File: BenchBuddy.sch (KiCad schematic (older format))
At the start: 0 parts

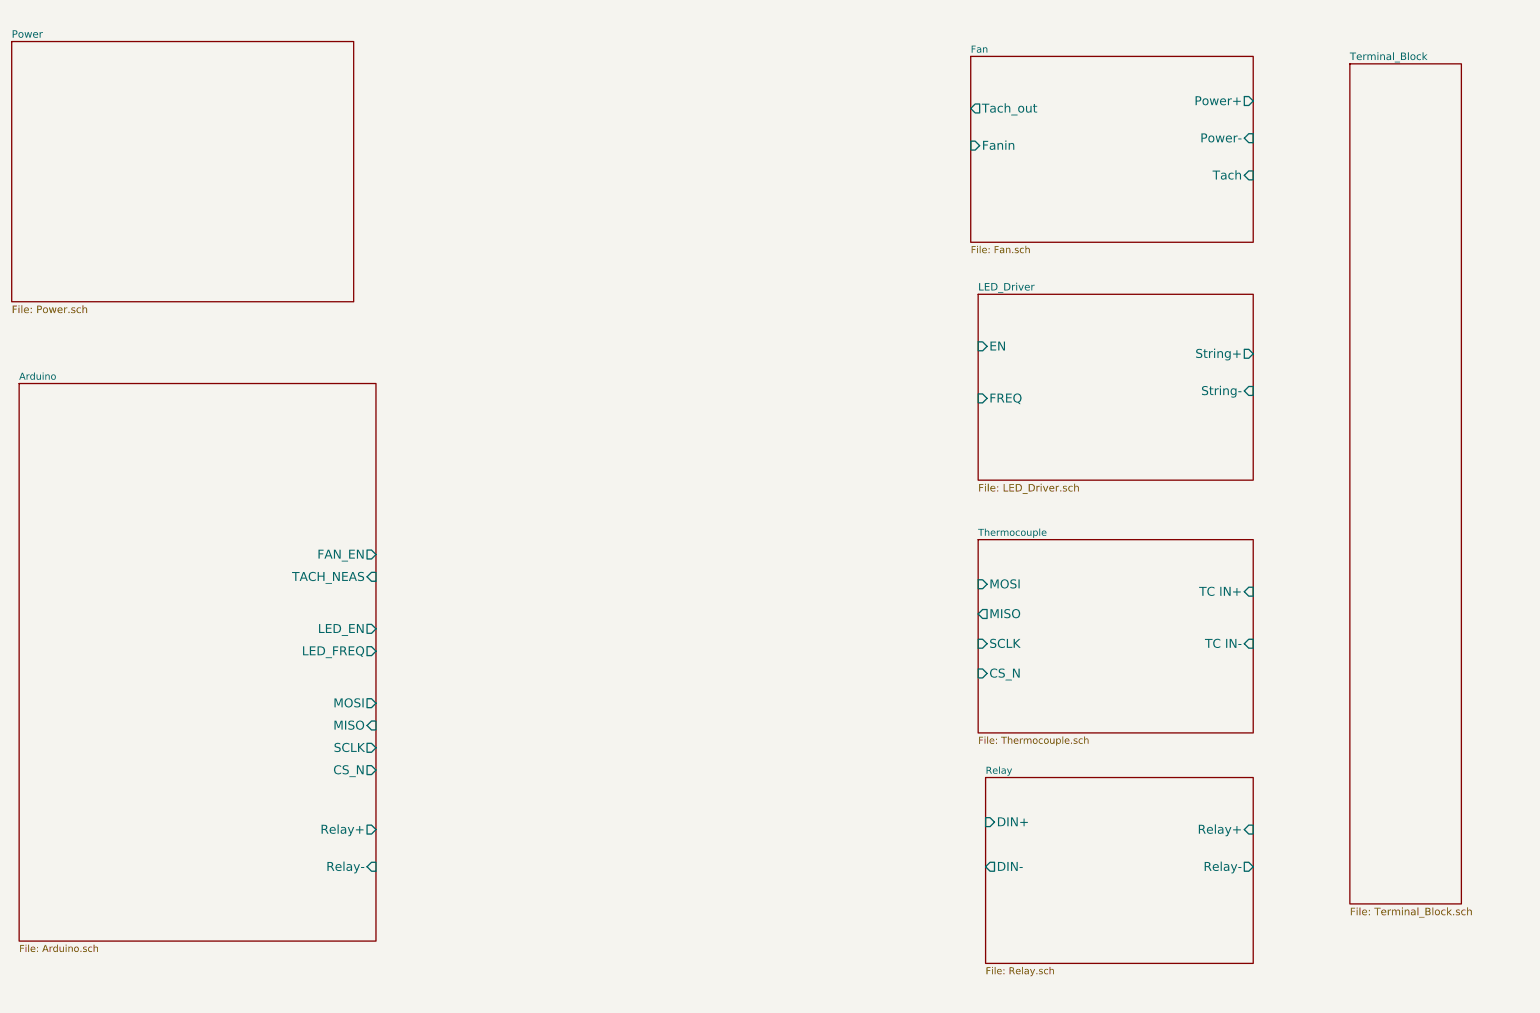
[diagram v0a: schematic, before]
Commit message: Added Powercontrol stuff
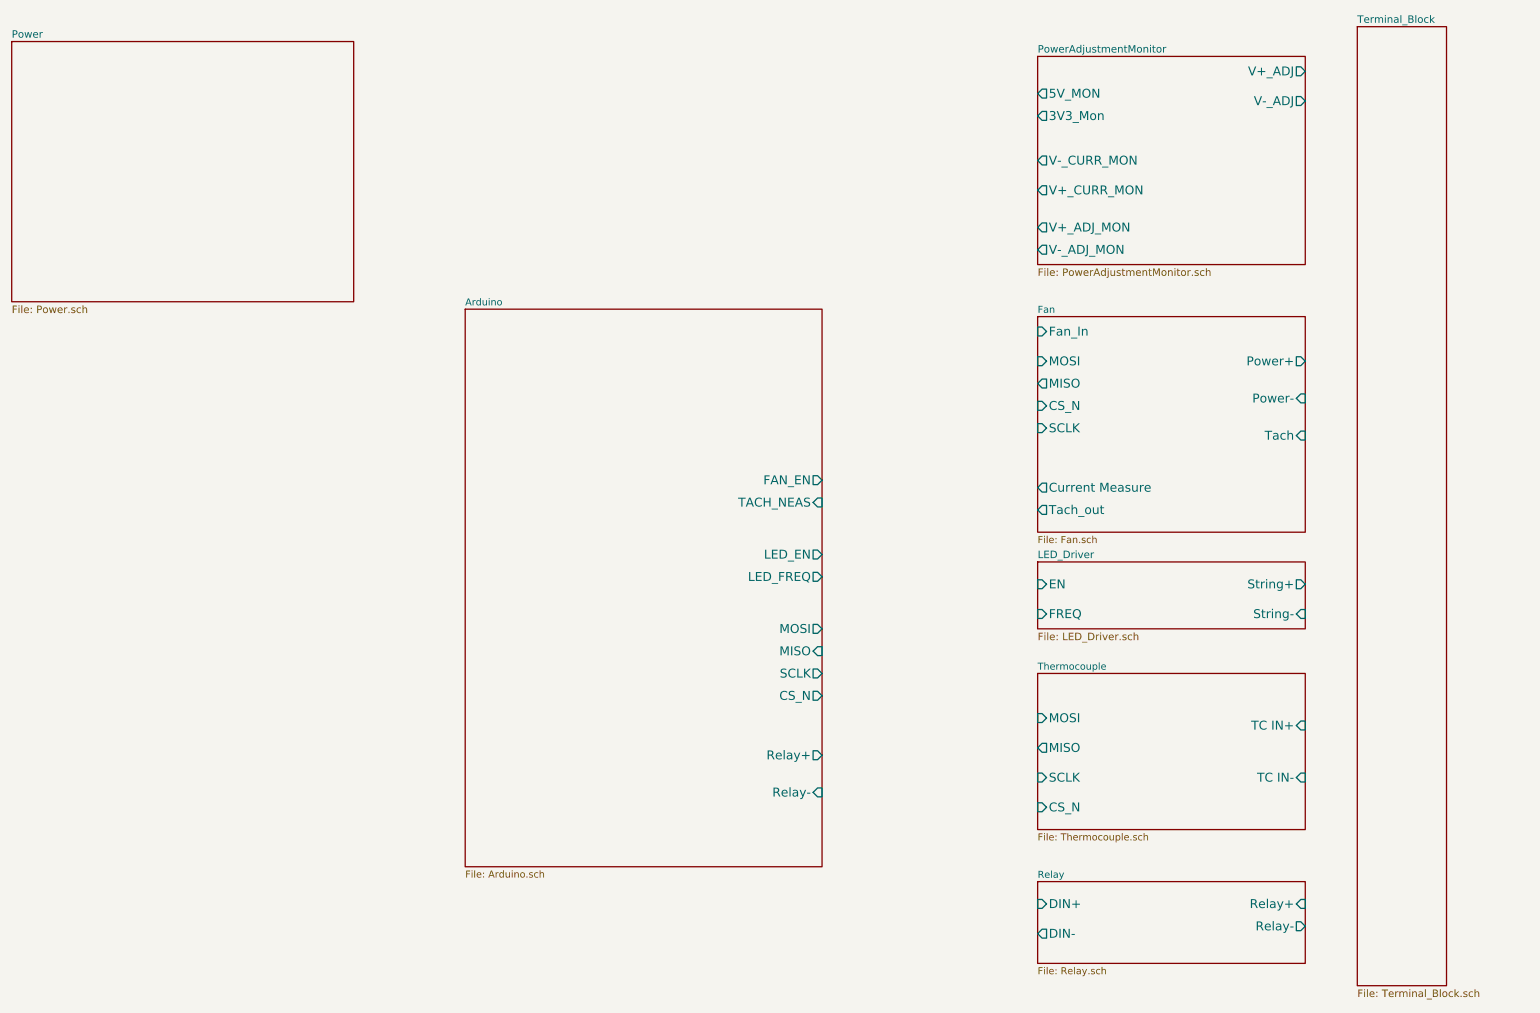
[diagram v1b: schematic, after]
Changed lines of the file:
@@
 LIBS:contrib
 LIBS:valves
+LIBS:BenchBuddy
 LIBS:BenchBuddy-cache
 EELAYER 27 0
@@
 $Descr A4 11693 8268
 encoding utf-8
-Sheet 1 8
+Sheet 1 9
 Title ""
-Date "31 jan 2014"
+Date "4 feb 2014"
 Rev ""
 Comp ""
@@
 $EndDescr
 $Sheet
-S 900  3000 2400 3750
+S 3900 2500 2400 3750
 U 52EBBFA9
 F0 "Arduino" 47
 F1 "Arduino.sch" 47
-F2 "Relay+" O R 3300 6000 60
-F3 "Relay-" I R 3300 6250 60
-F4 "MOSI" O R 3300 5150 60
-F5 "MISO" I R 3300 5300 60
-F6 "SCLK" O R 3300 5450 60
-F7 "CS_N" O R 3300 5600 60
-F8 "LED_EN" O R 3300 4650 60
-F9 "LED_FREQ" O R 3300 4800 60
-F10 "FAN_EN" O R 3300 4150 60
-F11 "TACH_NEAS" I R 3300 4300 60
+F2 "Relay+" O R 6300 5500 60
+F3 "Relay-" I R 6300 5750 60
+F4 "MOSI" O R 6300 4650 60
+F5 "MISO" I R 6300 4800 60
+F6 "SCLK" O R 6300 4950 60
+F7 "CS_N" O R 6300 5100 60
+F8 "LED_EN" O R 6300 4150 60
+F9 "LED_FREQ" O R 6300 4300 60
+F10 "FAN_EN" O R 6300 3650 60
+F11 "TACH_NEAS" I R 6300 3800 60
 $EndSheet
 $Sheet
-S 7350 4050 1850 1300
+S 7750 4950 1800 1050
 U 52EBC0AD
 F0 "Thermocouple" 47
 F1 "Thermocouple.sch" 47
-F2 "TC IN+" I R 9200 4400 60
-F3 "TC IN-" I R 9200 4750 60
-F4 "MOSI" I L 7350 4350 60
-F5 "MISO" O L 7350 4550 60
-F6 "SCLK" I L 7350 4750 60
-F7 "CS_N" I L 7350 4950 60
+F2 "TC IN+" I R 9550 5300 60
+F3 "TC IN-" I R 9550 5650 60
+F4 "MOSI" I L 7750 5250 60
+F5 "MISO" O L 7750 5450 60
+F6 "SCLK" I L 7750 5650 60
+F7 "CS_N" I L 7750 5850 60
 $EndSheet
 $Sheet
-S 7400 5650 1800 1250
+S 7750 6350 1800 550
 U 52EBC0CF
 F0 "Relay" 47
 F1 "Relay.sch" 47
-F2 "DIN+" I L 7400 5950 60
-F3 "DIN-" O L 7400 6250 60
-F4 "Relay-" O R 9200 6250 60
-F5 "Relay+" I R 9200 6000 60
+F2 "DIN+" I L 7750 6500 60
+F3 "DIN-" O L 7750 6700 60
+F4 "Relay-" O R 9550 6650 60
+F5 "Relay+" I R 9550 6500 60
 $EndSheet
 $Sheet
@@
 $EndSheet
 $Sheet
-S 7350 2400 1850 1250
+S 7750 4200 1800 450
 U 52EBC11D
 F0 "LED_Driver" 50
 F1 "LED_Driver.sch" 50
-F2 "EN" I L 7350 2750 60
-F3 "FREQ" I L 7350 3100 60
-F4 "String+" O R 9200 2800 60
-F5 "String-" I R 9200 3050 60
+F2 "EN" I L 7750 4350 60
+F3 "FREQ" I L 7750 4550 60
+F4 "String+" O R 9550 4350 60
+F5 "String-" I R 9550 4550 60
 $EndSheet
 $Sheet
-S 9850 850  750  5650
+S 9900 600  600  6450
 U 52EBC19C
 F0 "Terminal_Block" 50
@@
 $EndSheet
 $Sheet
-S 7300 800  1900 1250
+S 7750 2550 1800 1450
 U 52EBC1E0
 F0 "Fan" 47
 F1 "Fan.sch" 47
-F2 "Power+" O R 9200 1100 60
-F3 "Power-" I R 9200 1350 60
-F4 "Tach" I R 9200 1600 60
-F5 "Tach_out" O L 7300 1150 60
-F6 "Fanin" I L 7300 1400 60
+F2 "Power+" O R 9550 2850 60
+F3 "Power-" I R 9550 3100 60
+F4 "Tach" I R 9550 3350 60
+F5 "Tach_out" O L 7750 3850 60
+F6 "Fan_In" I L 7750 2650 60
+F7 "Current Measure" O L 7750 3700 60
+F8 "MOSI" I L 7750 2850 60
+F9 "MISO" O L 7750 3000 60
+F10 "CS_N" I L 7750 3150 60
+F11 "SCLK" I L 7750 3300 60
+$EndSheet
+$Sheet
+S 7750 800  1800 1400
+U 52F104D9
+F0 "PowerAdjustmentMonitor" 50
+F1 "PowerAdjustmentMonitor.sch" 50
+F2 "3V3_Mon" O L 7750 1200 60
+F3 "5V_MON" O L 7750 1050 60
+F4 "V+_ADJ_MON" O L 7750 1950 60
+F5 "V-_ADJ_MON" O L 7750 2100 60
+F6 "V-_CURR_MON" O L 7750 1500 60
+F7 "V+_CURR_MON" O L 7750 1700 60
+F8 "V-_ADJ" O R 9550 1100 60
+F9 "V+_ADJ" O R 9550 900 60
 $EndSheet
 $EndSCHEMATC

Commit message: Struktur nach Arduino
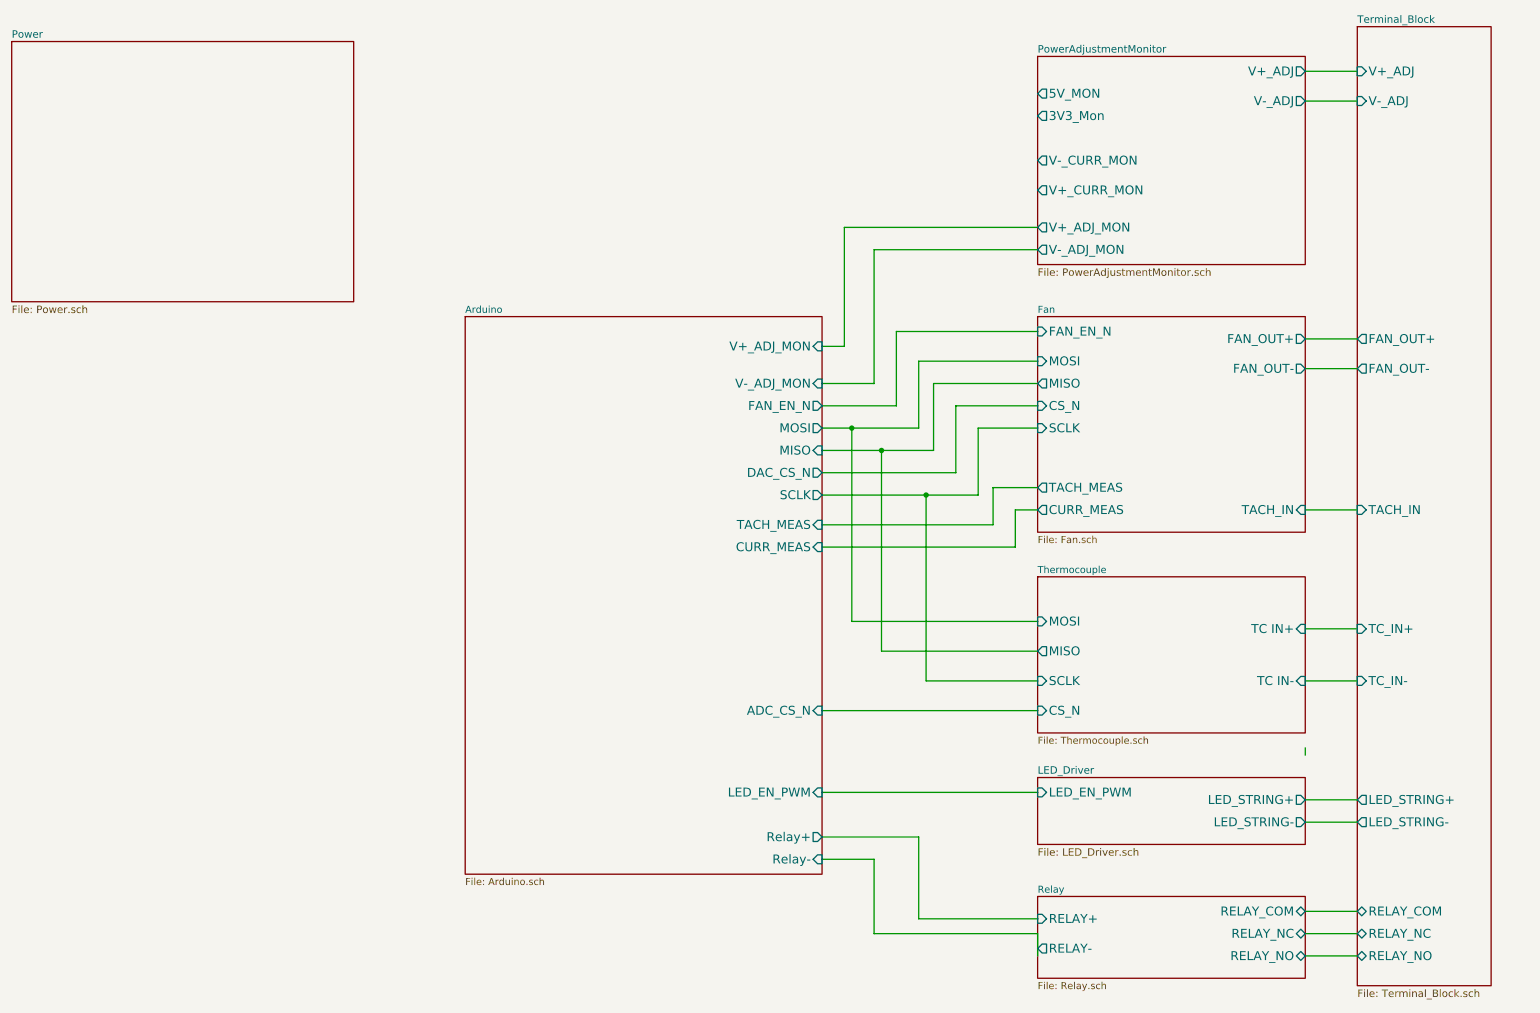
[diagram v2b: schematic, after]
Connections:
- wire segments 0 -> 55
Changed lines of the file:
@@
 Sheet 1 9
 Title ""
-Date "4 feb 2014"
+Date "6 feb 2014"
 Rev ""
 Comp ""
@@
 $EndDescr
 $Sheet
-S 3900 2500 2400 3750
-U 52EBBFA9
-F0 "Arduino" 47
-F1 "Arduino.sch" 47
-F2 "Relay+" O R 6300 5500 60
-F3 "Relay-" I R 6300 5750 60
-F4 "MOSI" O R 6300 4650 60
-F5 "MISO" I R 6300 4800 60
-F6 "SCLK" O R 6300 4950 60
-F7 "CS_N" O R 6300 5100 60
-F8 "LED_EN" O R 6300 4150 60
-F9 "LED_FREQ" O R 6300 4300 60
-F10 "FAN_EN" O R 6300 3650 60
-F11 "TACH_NEAS" I R 6300 3800 60
-$EndSheet
-$Sheet
-S 7750 4950 1800 1050
+S 7750 4300 1800 1050
 U 52EBC0AD
 F0 "Thermocouple" 47
 F1 "Thermocouple.sch" 47
-F2 "TC IN+" I R 9550 5300 60
-F3 "TC IN-" I R 9550 5650 60
-F4 "MOSI" I L 7750 5250 60
-F5 "MISO" O L 7750 5450 60
-F6 "SCLK" I L 7750 5650 60
-F7 "CS_N" I L 7750 5850 60
-$EndSheet
-$Sheet
-S 7750 6350 1800 550
+F2 "TC IN+" I R 9550 4650 60
+F3 "TC IN-" I R 9550 5000 60
+F4 "MOSI" I L 7750 4600 60
+F5 "MISO" O L 7750 4800 60
+F6 "SCLK" I L 7750 5000 60
+F7 "CS_N" I L 7750 5200 60
+$EndSheet
+$Sheet
+S 7750 6450 1800 550
 U 52EBC0CF
 F0 "Relay" 47
 F1 "Relay.sch" 47
-F2 "DIN+" I L 7750 6500 60
-F3 "DIN-" O L 7750 6700 60
-F4 "Relay-" O R 9550 6650 60
-F5 "Relay+" I R 9550 6500 60
+F2 "RELAY_NO" B R 9550 6850 60
+F3 "RELAY_NC" B R 9550 6700 60
+F4 "RELAY_COM" B R 9550 6550 60
+F5 "RELAY+" I L 7750 6600 60
+F6 "RELAY-" O L 7750 6800 60
 $EndSheet
 $Sheet
@@
 $EndSheet
 $Sheet
-S 7750 4200 1800 450
+S 7750 5650 1800 450
 U 52EBC11D
 F0 "LED_Driver" 50
 F1 "LED_Driver.sch" 50
-F2 "EN" I L 7750 4350 60
-F3 "FREQ" I L 7750 4550 60
-F4 "String+" O R 9550 4350 60
-F5 "String-" I R 9550 4550 60
-$EndSheet
-$Sheet
-S 9900 600  600  6450
+F2 "LED_EN_PWM" I L 7750 5750 60
+F3 "LED_STRING+" O R 9550 5800 60
+F4 "LED_STRING-" O R 9550 5950 60
+$EndSheet
+$Sheet
+S 9900 600  900  6450
 U 52EBC19C
 F0 "Terminal_Block" 50
 F1 "Terminal_Block.sch" 50
+F2 "V+_ADJ" I L 9900 900 60
+F3 "V-_ADJ" I L 9900 1100 60
+F4 "FAN_OUT+" O L 9900 2700 60
+F5 "FAN_OUT-" O L 9900 2900 60
+F6 "TACH_IN" I L 9900 3850 60
+F7 "LED_STRING+" O L 9900 5800 60
+F8 "LED_STRING-" O L 9900 5950 60
+F9 "TC_IN+" I L 9900 4650 60
+F10 "TC_IN-" I L 9900 5000 60
+F11 "RELAY_COM" B L 9900 6550 60
+F12 "RELAY_NC" B L 9900 6700 60
+F13 "RELAY_NO" B L 9900 6850 60
 $EndSheet
 $Sheet
@@
 F0 "Fan" 47
 F1 "Fan.sch" 47
-F2 "Power+" O R 9550 2850 60
-F3 "Power-" I R 9550 3100 60
-F4 "Tach" I R 9550 3350 60
-F5 "Tach_out" O L 7750 3850 60
-F6 "Fan_In" I L 7750 2650 60
-F7 "Current Measure" O L 7750 3700 60
-F8 "MOSI" I L 7750 2850 60
-F9 "MISO" O L 7750 3000 60
-F10 "CS_N" I L 7750 3150 60
-F11 "SCLK" I L 7750 3300 60
+F2 "MOSI" I L 7750 2850 60
+F3 "MISO" O L 7750 3000 60
+F4 "CS_N" I L 7750 3150 60
+F5 "SCLK" I L 7750 3300 60
+F6 "FAN_OUT+" O R 9550 2700 60
+F7 "FAN_OUT-" O R 9550 2900 60
+F8 "TACH_IN" I R 9550 3850 60
+F9 "TACH_MEAS" O L 7750 3700 60
+F10 "FAN_EN_N" I L 7750 2650 60
+F11 "CURR_MEAS" O L 7750 3850 60
 $EndSheet
 $Sheet
@@
 F9 "V+_ADJ" O R 9550 900 60
 $EndSheet
+Wire Wire Line
+	9900 900  9550 900
+Wire Wire Line
+	9550 1100 9900 1100
+Wire Wire Line
+	9900 2700 9550 2700
+Wire Wire Line
+	9550 2900 9900 2900
+Wire Wire Line
+	9900 3850 9550 3850
+Wire Wire Line
+	6300 2750 6450 2750
+Wire Wire Line
+	6450 2750 6450 1950
+Wire Wire Line
+	6450 1950 7750 1950
+Wire Wire Line
+	6300 3000 6650 3000
+Wire Wire Line
+	6650 3000 6650 2100
+Wire Wire Line
+	6650 2100 7750 2100
+Wire Wire Line
+	6300 3150 6800 3150
+Wire Wire Line
+	6800 3150 6800 2650
+Wire Wire Line
+	6800 2650 7750 2650
+Wire Wire Line
+	6300 3300 6950 3300
+Wire Wire Line
+	6950 3300 6950 2850
+Wire Wire Line
+	6950 2850 7750 2850
+Wire Wire Line
+	6300 3450 7050 3450
+Wire Wire Line
+	7050 3450 7050 3000
+Wire Wire Line
+	7050 3000 7750 3000
+Wire Wire Line
+	6300 3950 7450 3950
+Wire Wire Line
+	7450 3950 7450 3700
+Wire Wire Line
+	7450 3700 7750 3700
+Wire Wire Line
+	7750 3850 7600 3850
+Wire Wire Line
+	7600 3850 7600 4100
+Wire Wire Line
+	7600 4100 6300 4100
+Wire Wire Line
+	9550 5500 9550 5450
+Wire Wire Line
+	9550 4650 9900 4650
+Wire Wire Line
+	9900 5000 9550 5000
+Wire Wire Line
+	9900 5800 9550 5800
+Wire Wire Line
+	9550 5950 9900 5950
+Wire Wire Line
+	9900 6550 9550 6550
+Wire Wire Line
+	9550 6700 9900 6700
+Wire Wire Line
+	9900 6850 9550 6850
+Wire Wire Line
+	7750 4600 6500 4600
+Wire Wire Line
+	6500 4600 6500 3300
+Connection ~ 6500 3300
+Wire Wire Line
+	7750 4800 6700 4800
+Wire Wire Line
+	6700 4800 6700 3450
+Connection ~ 6700 3450
+$Sheet
+S 3900 2550 2400 3750
+U 52EBBFA9
+F0 "Arduino" 47
+F1 "Arduino.sch" 47
+F2 "Relay+" O R 6300 6050 60
+F3 "Relay-" I R 6300 6200 60
+F4 "MOSI" O R 6300 3300 60
+F5 "MISO" I R 6300 3450 60
+F6 "SCLK" O R 6300 3750 60
+F7 "TACH_MEAS" I R 6300 3950 60
+F8 "FAN_EN_N" O R 6300 3150 60
+F9 "CURR_MEAS" I R 6300 4100 60
+F10 "V+_ADJ_MON" I R 6300 2750 60
+F11 "V-_ADJ_MON" I R 6300 3000 60
+F12 "LED_EN_PWM" I R 6300 5750 60
+F13 "DAC_CS_N" O R 6300 3600 60
+F14 "ADC_CS_N" I R 6300 5200 60
+$EndSheet
+Wire Wire Line
+	7750 3150 7200 3150
+Wire Wire Line
+	7200 3150 7200 3600
+Wire Wire Line
+	7200 3600 6300 3600
+Wire Wire Line
+	7750 3300 7350 3300
+Wire Wire Line
+	7350 3300 7350 3750
+Wire Wire Line
+	7350 3750 6300 3750
+Wire Wire Line
+	7750 5000 7000 5000
+Wire Wire Line
+	7000 5000 7000 3750
+Connection ~ 7000 3750
+Wire Wire Line
+	7750 5200 6300 5200
+Wire Wire Line
+	7750 5750 6300 5750
+Wire Wire Line
+	6300 6050 6950 6050
+Wire Wire Line
+	6950 6050 6950 6600
+Wire Wire Line
+	6950 6600 7750 6600
+Wire Wire Line
+	7750 6850 7750 6700
+Wire Wire Line
+	7750 6700 6650 6700
+Wire Wire Line
+	6650 6700 6650 6200
+Wire Wire Line
+	6650 6200 6300 6200
 $EndSCHEMATC
